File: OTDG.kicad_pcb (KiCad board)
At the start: 2 copper layers, 86.1 x 39.9 mm, 52 parts, among them J1 Raspberry_Pi_2_3, J10 Conn_01x02_Female, J11 Conn_01x02_Female, J12 Conn_01x02_Female, J13 Conn_01x02_Female, J14 Conn_01x02_Male, J15 Conn_01x02_Male, J16 Conn_01x02_Male, J17 Conn_01x02_Male, J18 Conn_01x02_Male, J19 Conn_01x02_Male, J2 Conn_01x02_Female, J20 Conn_01x02_Male, J21 Conn_01x02_Male, J22 Conn_01x02_Male, J3 Conn_01x02_Female, J4 Conn_01x02_Female, J5 Conn_01x02_Female, J6 Conn_01x02_Female, J7 Conn_01x02_Female, J8 Conn_01x02_Female, J9 Conn_01x02_Female, SW1 SW_Push_Dual, SW2 SW_Push_Dual, SW3 SW_Push_Dual, SW4 SW_Push_Dual, SW5 SW_Push_Dual, SW6 SW_Push_Dual, SW7 SW_Push_Dual, SW8 SW_Push_Dual, SW9 SW_Push_Dual

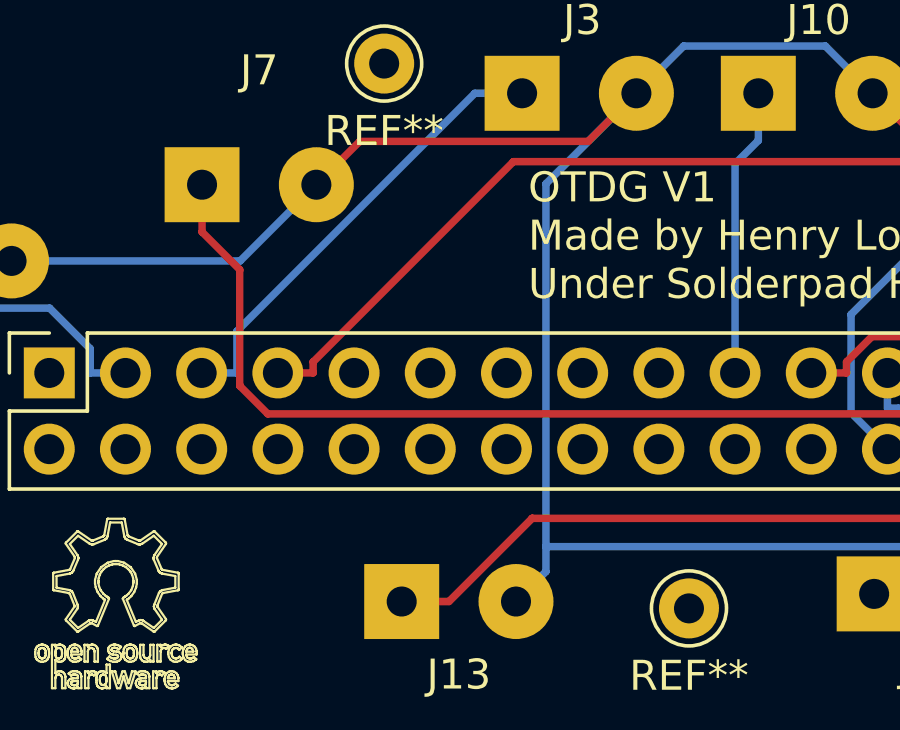
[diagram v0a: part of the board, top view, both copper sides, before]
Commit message: Connected ground, added README
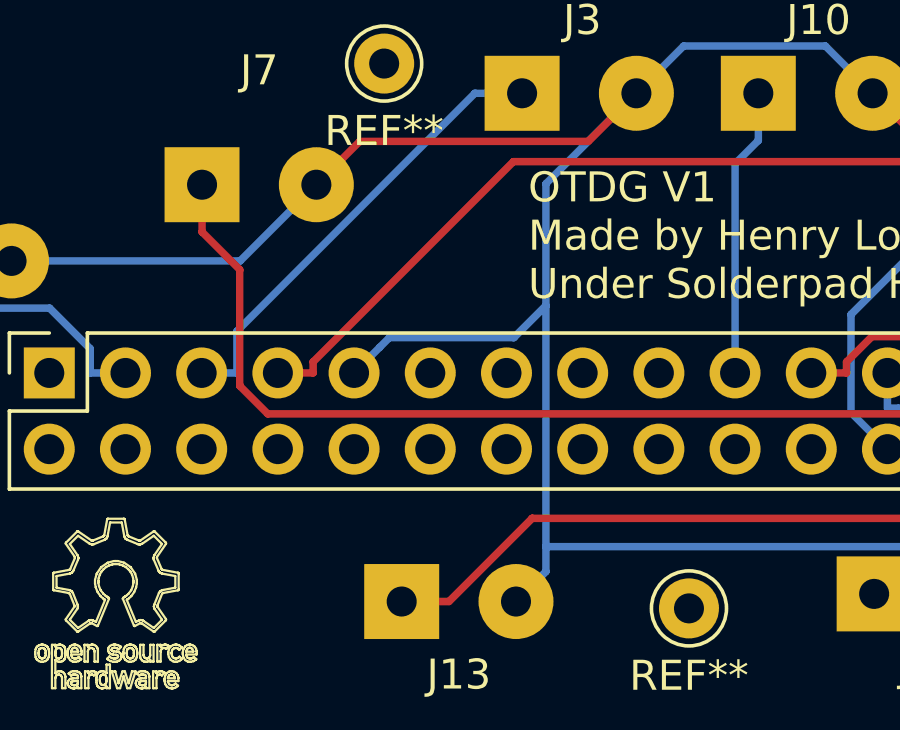
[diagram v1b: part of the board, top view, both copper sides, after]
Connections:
- J1 pad 9: Net-(J1-Pad9) -> GND
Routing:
- net GND: track 122.9 -> 130.2 mm
